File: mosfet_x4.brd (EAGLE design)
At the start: 72.1 x 30.5 mm, 26 parts, among them Q1 IRLZ34N, Q2 IRLZ34N, Q3 IRLZ34N, Q4 IRLZ34N

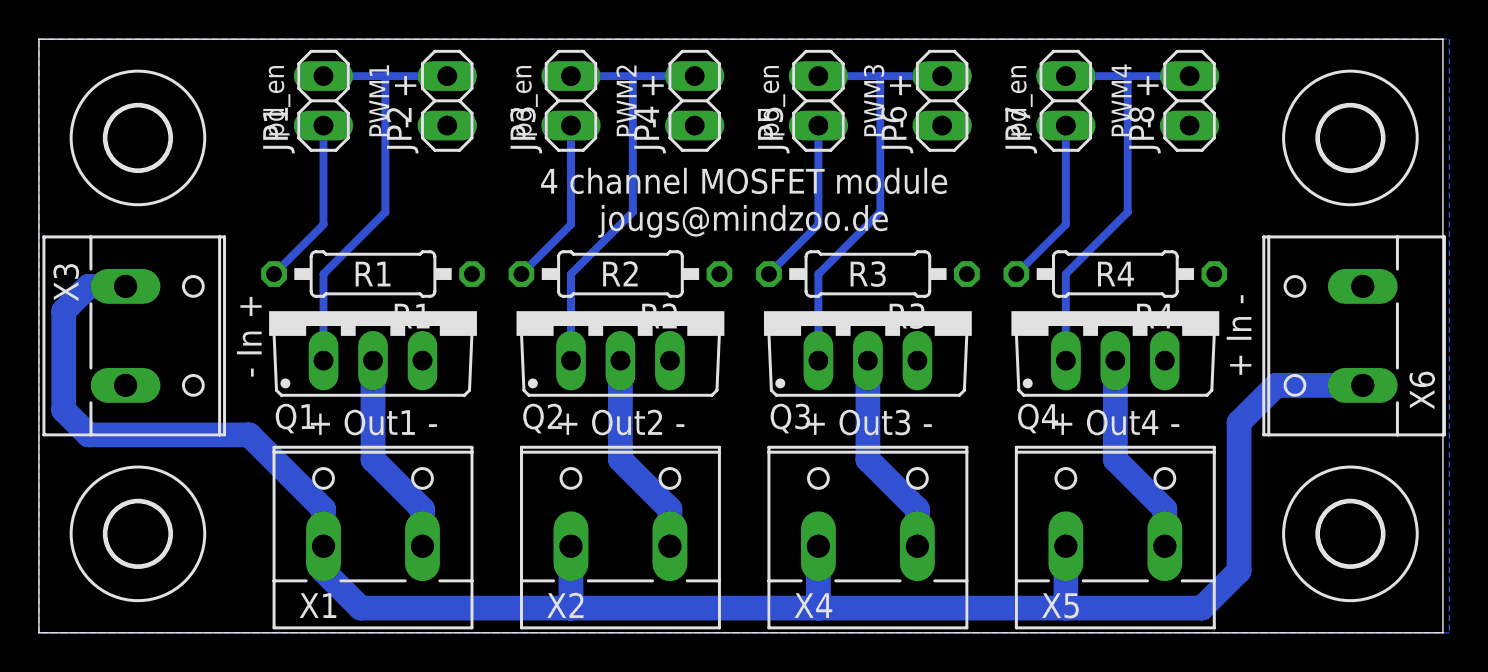
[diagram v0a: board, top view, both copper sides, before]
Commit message: Added second layer with ground plate
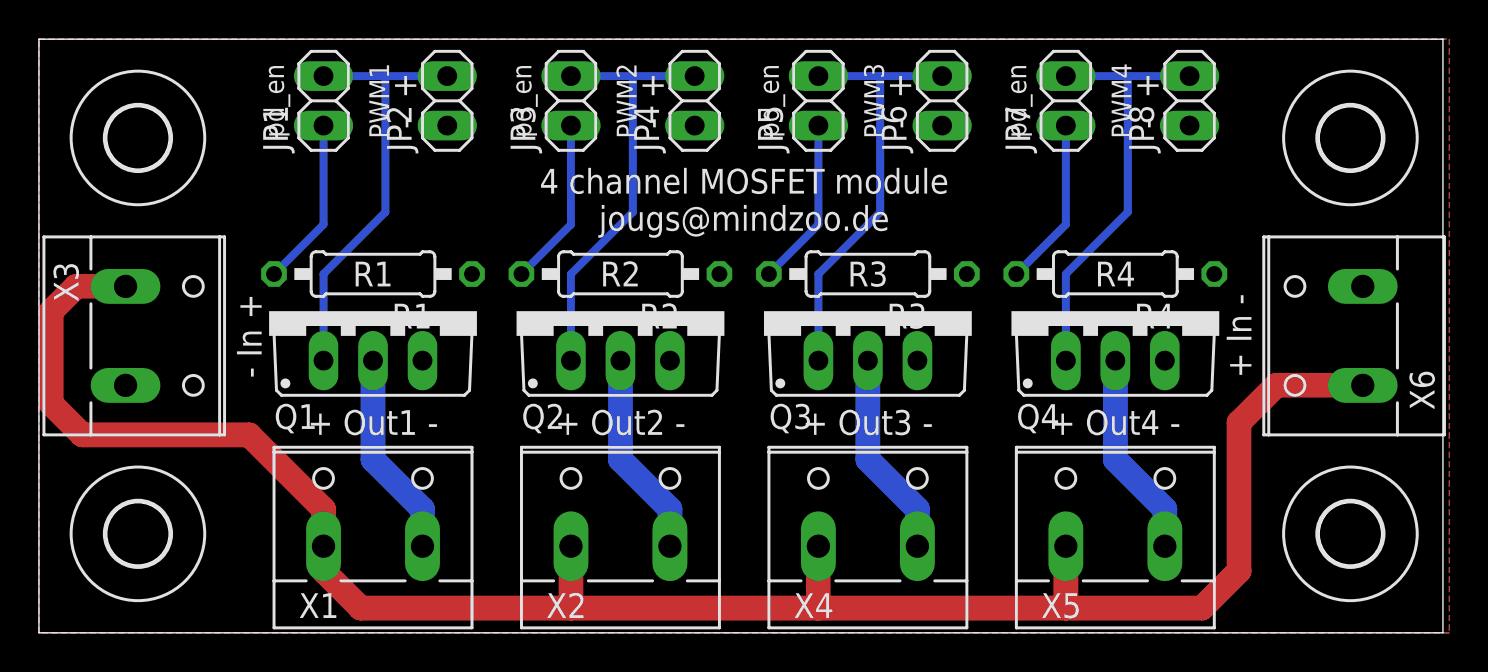
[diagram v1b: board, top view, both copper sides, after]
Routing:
- net +12V: track 100.2 -> 101.3 mm
- added copper zone on layer 1, net GND
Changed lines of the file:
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@@
 <?xml version="1.0" encoding="utf-8"?>
 <!DOCTYPE eagle SYSTEM "eagle.dtd">
-<eagle version="6.6.0">
+<eagle version="7.6.0">
 <drawing>
 <settings>
@@
 <pass name="Default">
 <param name="RoutingGrid" value="50mil"/>
+<param name="AutoGrid" value="1"/>
+<param name="Efforts" value="0"/>
+<param name="TopRouterVariant" value="1"/>
 <param name="tpViaShape" value="round"/>
 <param name="PrefDir.1" value="|"/>
@@
 <vertex x="0" y="0"/>
 </polygon>
+<polygon width="0.4064" layer="1">
+<vertex x="0" y="30.48"/>
+<vertex x="72.39" y="30.48"/>
+<vertex x="72.39" y="0"/>
+<vertex x="0" y="0"/>
+</polygon>
 </signal>
 <signal name="N$1">
@@
 <contactref element="X1" pad="1"/>
 <contactref element="X3" pad="1"/>
-<wire x1="4.445" y1="17.78" x2="2.54" y2="17.78" width="1.27" layer="16"/>
-<wire x1="2.54" y1="17.78" x2="1.27" y2="16.51" width="1.27" layer="16"/>
-<wire x1="1.27" y1="16.51" x2="1.27" y2="11.43" width="1.27" layer="16"/>
-<wire x1="1.27" y1="11.43" x2="2.54" y2="10.16" width="1.27" layer="16"/>
-<wire x1="2.54" y1="10.16" x2="10.795" y2="10.16" width="1.27" layer="16"/>
-<wire x1="10.795" y1="10.16" x2="14.605" y2="6.35" width="1.27" layer="16"/>
-<wire x1="14.605" y1="6.35" x2="14.605" y2="4.445" width="1.27" layer="16"/>
-<wire x1="14.605" y1="4.445" x2="14.605" y2="3.175" width="1.27" layer="16"/>
-<wire x1="14.605" y1="3.175" x2="16.51" y2="1.27" width="1.27" layer="16"/>
-<wire x1="16.51" y1="1.27" x2="27.305" y2="1.27" width="1.27" layer="16"/>
+<wire x1="0.635" y1="11.7475" x2="0.635" y2="16.51" width="1.27" layer="1"/>
+<wire x1="0.635" y1="16.51" x2="1.905" y2="17.78" width="1.27" layer="1"/>
+<wire x1="1.905" y1="17.78" x2="4.445" y2="17.78" width="1.27" layer="1"/>
+<wire x1="0.635" y1="11.7475" x2="2.2225" y2="10.16" width="1.27" layer="1"/>
+<wire x1="2.2225" y1="10.16" x2="10.795" y2="10.16" width="1.27" layer="1"/>
+<wire x1="10.795" y1="10.16" x2="14.605" y2="6.35" width="1.27" layer="1"/>
+<wire x1="14.605" y1="6.35" x2="14.605" y2="4.445" width="1.27" layer="1"/>
+<wire x1="14.605" y1="4.445" x2="14.605" y2="3.175" width="1.27" layer="1"/>
+<wire x1="14.605" y1="3.175" x2="16.51" y2="1.27" width="1.27" layer="1"/>
+<wire x1="16.51" y1="1.27" x2="27.305" y2="1.27" width="1.27" layer="1"/>
 <contactref element="X2" pad="1"/>
 <contactref element="X4" pad="1"/>
 <contactref element="X5" pad="1"/>
 <contactref element="X6" pad="1"/>
-<wire x1="27.305" y1="1.27" x2="40.005" y2="1.27" width="1.27" layer="16"/>
-<wire x1="40.005" y1="1.27" x2="52.705" y2="1.27" width="1.27" layer="16"/>
-<wire x1="52.705" y1="1.27" x2="59.69" y2="1.27" width="1.27" layer="16"/>
-<wire x1="27.305" y1="4.445" x2="27.305" y2="1.27" width="1.27" layer="16"/>
-<wire x1="40.005" y1="4.445" x2="40.005" y2="1.27" width="1.27" layer="16"/>
-<wire x1="52.705" y1="4.445" x2="52.705" y2="1.27" width="1.27" layer="16"/>
-<wire x1="67.945" y1="12.7" x2="63.5" y2="12.7" width="1.27" layer="16"/>
-<wire x1="63.5" y1="12.7" x2="61.595" y2="10.795" width="1.27" layer="16"/>
-<wire x1="61.595" y1="10.795" x2="61.595" y2="3.175" width="1.27" layer="16"/>
-<wire x1="61.595" y1="3.175" x2="59.69" y2="1.27" width="1.27" layer="16"/>
+<wire x1="27.305" y1="1.27" x2="40.005" y2="1.27" width="1.27" layer="1"/>
+<wire x1="40.005" y1="1.27" x2="52.705" y2="1.27" width="1.27" layer="1"/>
+<wire x1="52.705" y1="1.27" x2="59.69" y2="1.27" width="1.27" layer="1"/>
+<wire x1="27.305" y1="4.445" x2="27.305" y2="1.27" width="1.27" layer="1"/>
+<wire x1="40.005" y1="4.445" x2="40.005" y2="1.27" width="1.27" layer="1"/>
+<wire x1="52.705" y1="4.445" x2="52.705" y2="1.27" width="1.27" layer="1"/>
+<wire x1="67.945" y1="12.7" x2="63.5" y2="12.7" width="1.27" layer="1"/>
+<wire x1="63.5" y1="12.7" x2="61.595" y2="10.795" width="1.27" layer="1"/>
+<wire x1="61.595" y1="10.795" x2="61.595" y2="3.175" width="1.27" layer="1"/>
+<wire x1="61.595" y1="3.175" x2="59.69" y2="1.27" width="1.27" layer="1"/>
 </signal>
 <signal name="N$5">
